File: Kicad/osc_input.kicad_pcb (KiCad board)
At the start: 2 copper layers, 18 parts, among them Q1 BC547b, Q2 BC547b, U1 LM2931A

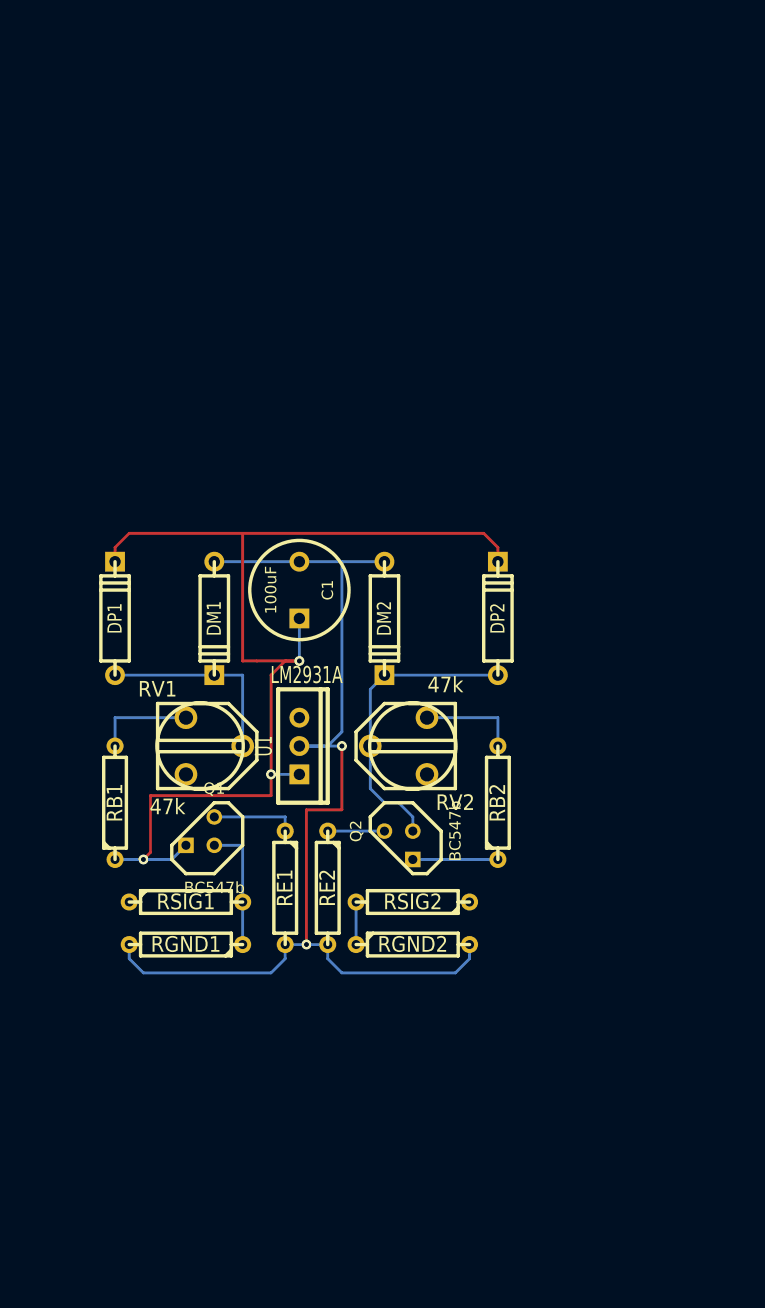
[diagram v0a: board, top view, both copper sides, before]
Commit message: Kicad: Updated to fit kicad version 4.0.4. Modified routing for next prototype.
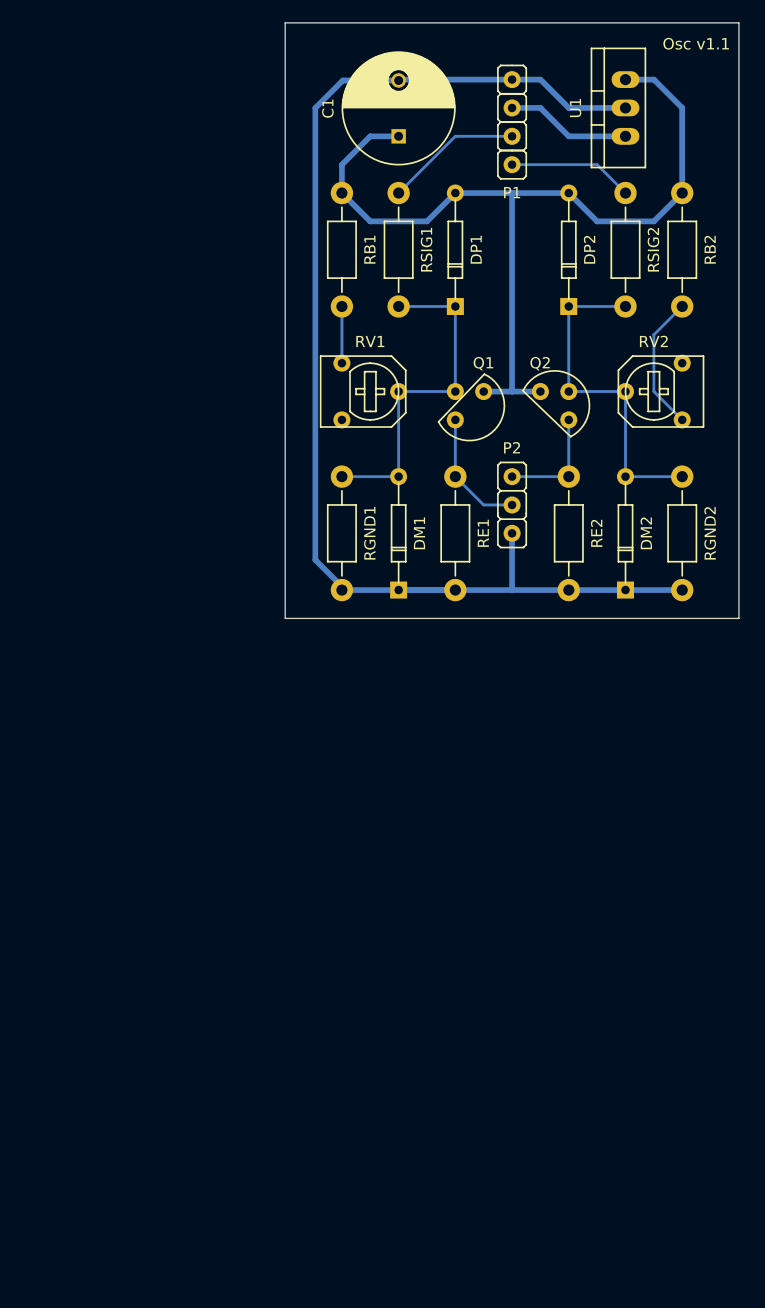
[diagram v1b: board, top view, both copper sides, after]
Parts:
- added P1: CONN_01X04, boul51:PinHeader_x4, F.Cu at (177.8, 25.4)
- added P2: CONN_01X03, boul51:PinHeader_x3, F.Cu at (177.8, 61.0)
- C1: footprint C2V8 -> Capacitors_THT:C_Radial_D10_L20_P5
- DM1, DM2, DP1, DP2: value 1n4007 -> 1N4007; footprint D4 -> boul51:Diode-DO41
- Q1: footprint TO92 -> boul51:TO-92_1
- Q2: footprint TO92 -> boul51:TO-92_2
- RB1, RB2, RGND1, RGND2, RSIG1, RSIG2: footprint R4 -> Resistors_THT:Resistor_Horizontal_RM10mm
- RE1, RE2: value 820 -> 1k; footprint R4 -> Resistors_THT:Resistor_Horizontal_RM10mm
- RV1, RV2: footprint RV2X3 -> boul51:Pot_5x8mm
- U1: footprint TO220_LM2931A -> TO_SOT_Packages_THT:TO-220_Neutral123_Vertical
- moved RSIG2 66.3 mm to (188.0, 33.0), turned to 270 degrees
- moved RSIG1 66.3 mm to (167.6, 33.0), turned to 270 degrees
- moved U1 64.2 mm to (188.0, 25.4), turned to 90 degrees
- moved RB1 58.3 mm to (162.6, 33.0), turned to 270 degrees
- moved RB2 57.1 mm to (193.0, 33.0), turned to 270 degrees
- moved RGND2 48.4 mm to (193.0, 58.4), turned to 270 degrees
- moved Q1 46.9 mm to (175.3, 50.8)
- moved DP1 44.9 mm to (172.7, 38.1)
- moved RGND1 44.2 mm to (162.6, 58.4), turned to 270 degrees
- moved RE2 42.7 mm to (182.9, 58.4)
- moved Q2 42.6 mm to (180.3, 50.8)
- moved C1 41.6 mm to (167.6, 27.9)
- moved RE1 39.9 mm to (172.7, 58.4)
- moved RV2 37.7 mm to (190.5, 50.8), turned to 90 degrees
- moved RV1 35.8 mm to (165.1, 50.8), turned to 270 degrees
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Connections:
- RSIG1 pad 1: (no net) -> VIN1
- RSIG2 pad 1: (no net) -> VIN2
- U1 pad 1: (no net) -> VCC
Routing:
- net VSTABLE: track 105.9 -> 80.0 mm, vias 3 -> 0
- net GND: track 97.2 -> 114.7 mm, vias 2 -> 0
- net VIN1: track 0.00 -> 12.3 mm
- net VCC: track 0.00 -> 11.2 mm
- net VIN2: track 0.00 -> 11.2 mm
- net VOUT2: track 5.08 -> 10.2 mm
- net Net-(RB1-Pad2): track 8.89 -> 5.08 mm
- net VOUT1: track 7.62 -> 11.2 mm
- net Net-(RB2-Pad2): track 8.89 -> 12.3 mm
- net VB1: track 29.2 -> 30.5 mm
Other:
- board outline added: 40.6 x 53.3 mm
- net class Power added: clearance 0.508, trace_width 0.508, via_dia 0.889, via_drill 0.635
- board text added: "Osc v1.1"

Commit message: Kicad: Added gitignore Updated text properties in pcb Use lib from boul51.lib (removed components_sch.lib)
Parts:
- moved DP1 64.1 mm to (149.2, 97.8)
- moved DP2 64.1 mm to (159.4, 97.8)
- moved P1 64.1 mm to (154.3, 85.1)
- moved P2 64.1 mm to (154.3, 120.7)
- moved U1 64.1 mm to (164.5, 85.1)
- moved DM2 64.1 mm to (164.5, 123.2)
- moved Q1 64.1 mm to (151.8, 110.5)
- moved Q2 64.1 mm to (156.8, 110.5)
- moved RE1 64.1 mm to (149.2, 118.1)
- moved RE2 64.1 mm to (159.4, 118.1)
- moved RGND1 64.1 mm to (139.1, 118.1)
- moved RGND2 64.1 mm to (169.5, 118.1)
- moved RV1 64.1 mm to (141.6, 110.5)
- moved RV2 64.1 mm to (167.0, 110.5)
- moved C1 64.1 mm to (144.1, 87.6)
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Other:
- board text added: "Picacilo v1.1"
- board text removed: "Osc v1.1"
